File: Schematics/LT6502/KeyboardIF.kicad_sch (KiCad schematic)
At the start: 7 parts, among them J14 KeyConn, U11 W65C51NxQ, X2 1.8432MHz

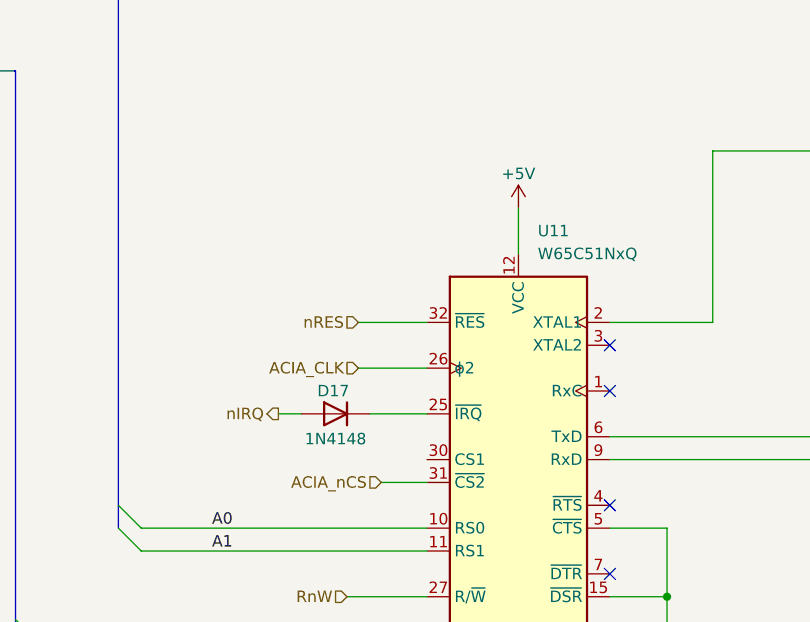
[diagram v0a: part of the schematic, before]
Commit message: Further work on Schematics, All parts placed on PCB
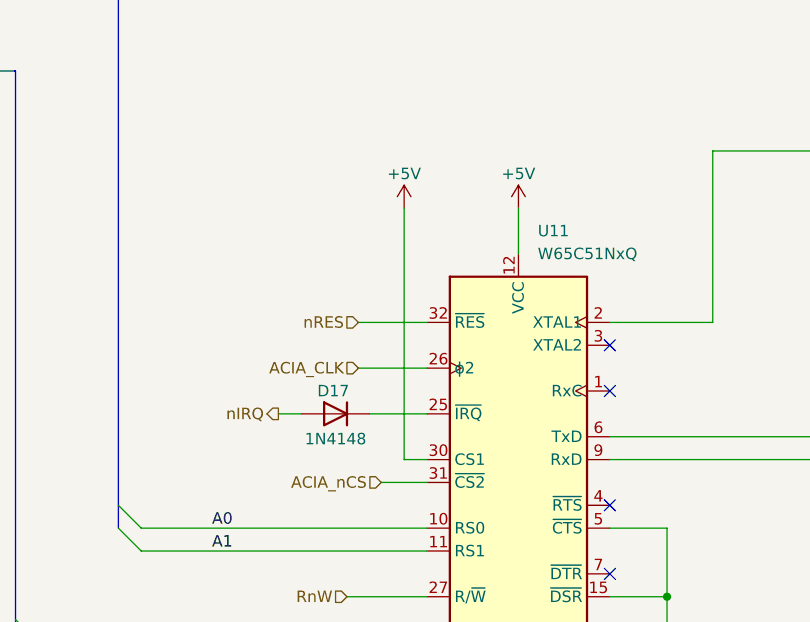
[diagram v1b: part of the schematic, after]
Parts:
- R82: footprint Resistor_SMD:R_0603_1608Metric_Pad0.98x0.95mm_HandSolder -> Resistor_SMD:R_0402_1005Metric
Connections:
- net +5V: now also U11.30 (CS1)
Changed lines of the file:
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@@
+	(wire
+		(pts
+			(xy 135.89 93.98) (xy 135.89 66.04)
+		)
+		(stroke
+			(width 0)
+			(type default)
+		)
+	)
 	(wire
 		(pts
@@
 		(pts
 			(xy 95.25 116.84) (xy 138.43 116.84)
+		)
+		(stroke
+			(width 0)
+			(type default)
+		)
+	)
+	(wire
+		(pts
+			(xy 138.43 93.98) (xy 135.89 93.98)
 		)
 		(stroke
@@
 			)
 		)
-		(property "Footprint" "Resistor_SMD:R_0603_1608Metric_Pad0.98x0.95mm_HandSolder"
+		(property "Footprint" "Resistor_SMD:R_0402_1005Metric"
 			(at 205.232 52.07 90)
 			(effects
@@
 					(unit 1)
 				)
+			)
+		)
+	)
+	(symbol
+		(lib_id "power:+5V")
+		(at 135.89 66.04 0)
+		(mirror y)
+		(unit 1)
+		(exclude_from_sim no)
+		(in_bom yes)
+		(on_board yes)
+		(dnp no)
+		(property "Reference" "#PWR0228"
+			(at 135.89 69.85 0)
+			(effects
+				(font
+					(size 1.27 1.27)
+				)
+				(hide yes)
+			)
+		)
+		(property "Value" "+5V"
+			(at 135.89 62.23 0)
+			(effects
+				(font
+					(size 1.27 1.27)
+				)
+			)
+		)
+		(property "Footprint" ""
+			(at 135.89 66.04 0)
+			(effects
+				(font
+					(size 1.27 1.27)
+				)
+				(hide yes)
+			)
+		)
+		(property "Datasheet" ""
+			(at 135.89 66.04 0)
+			(effects
+				(font
+					(size 1.27 1.27)
+				)
+				(hide yes)
+			)
+		)
+		(property "Description" ""
+			(at 135.89 66.04 0)
+			(effects
+				(font
+					(size 1.27 1.27)
+				)
+			)
+		)
+		(pin "1"
+		)
+		(instances
+			(project "LT6502"
+				(path "/a2243a34-697c-4939-97f7-df548e421864/2b6fed47-3df7-424e-b6fe-61f4842b9a70"
+					(reference "#PWR0228")
+					(unit 1)
+				)

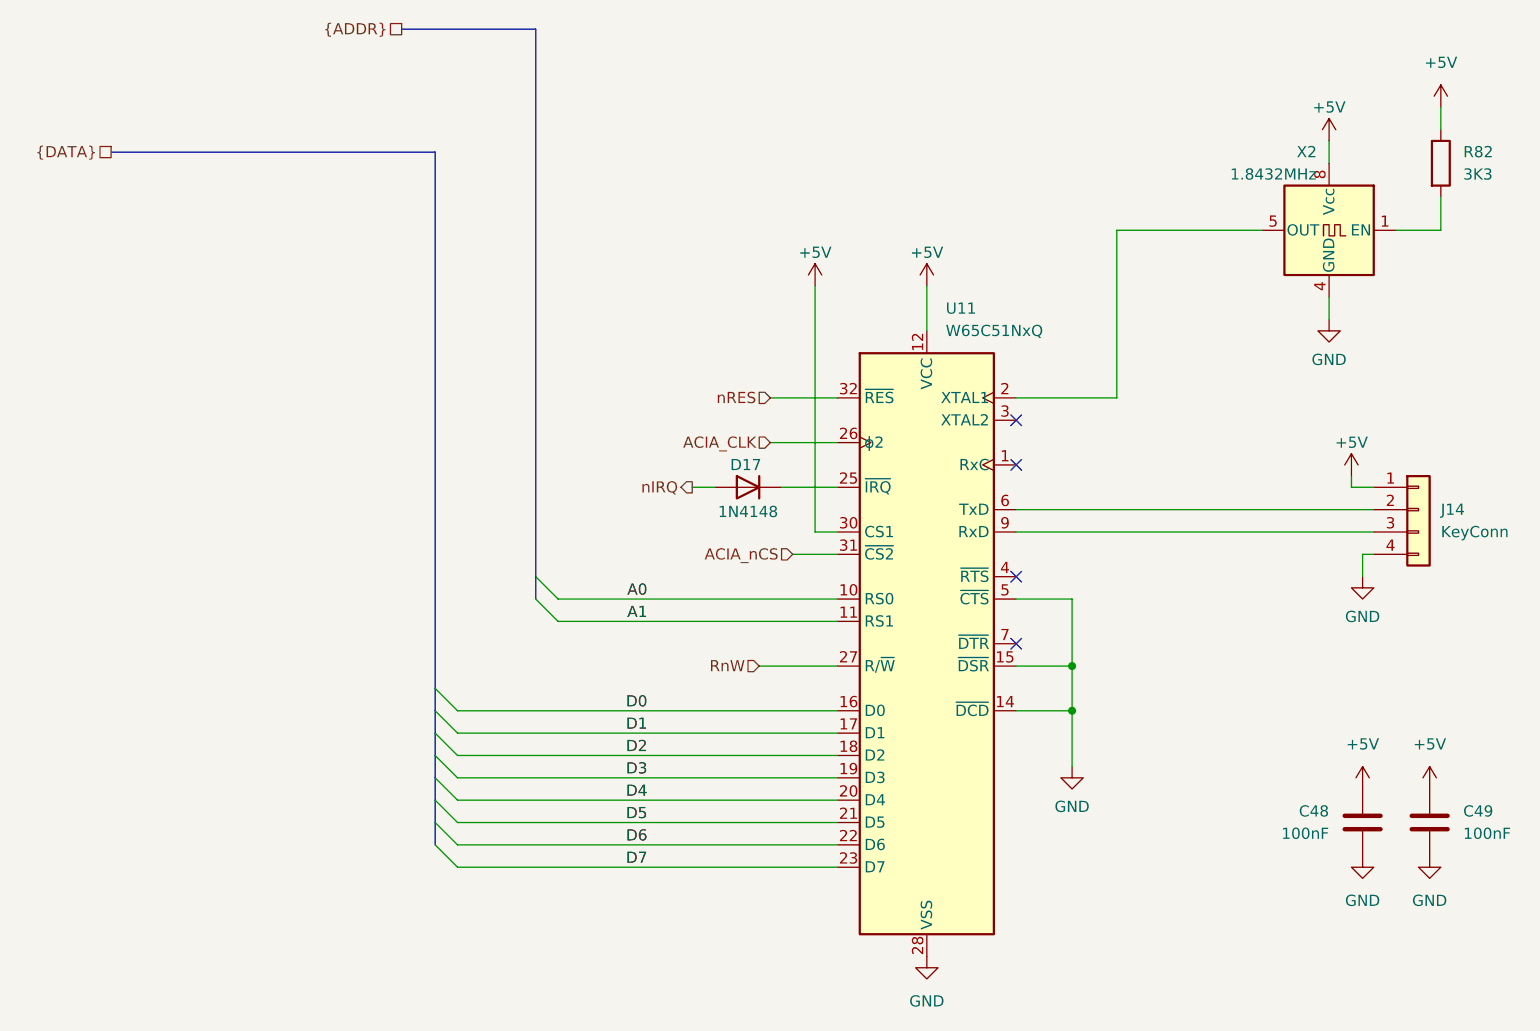
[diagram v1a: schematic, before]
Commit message: Updated main board and started keybed
main board a bit wider due to keybed width
created keybed, begun routing
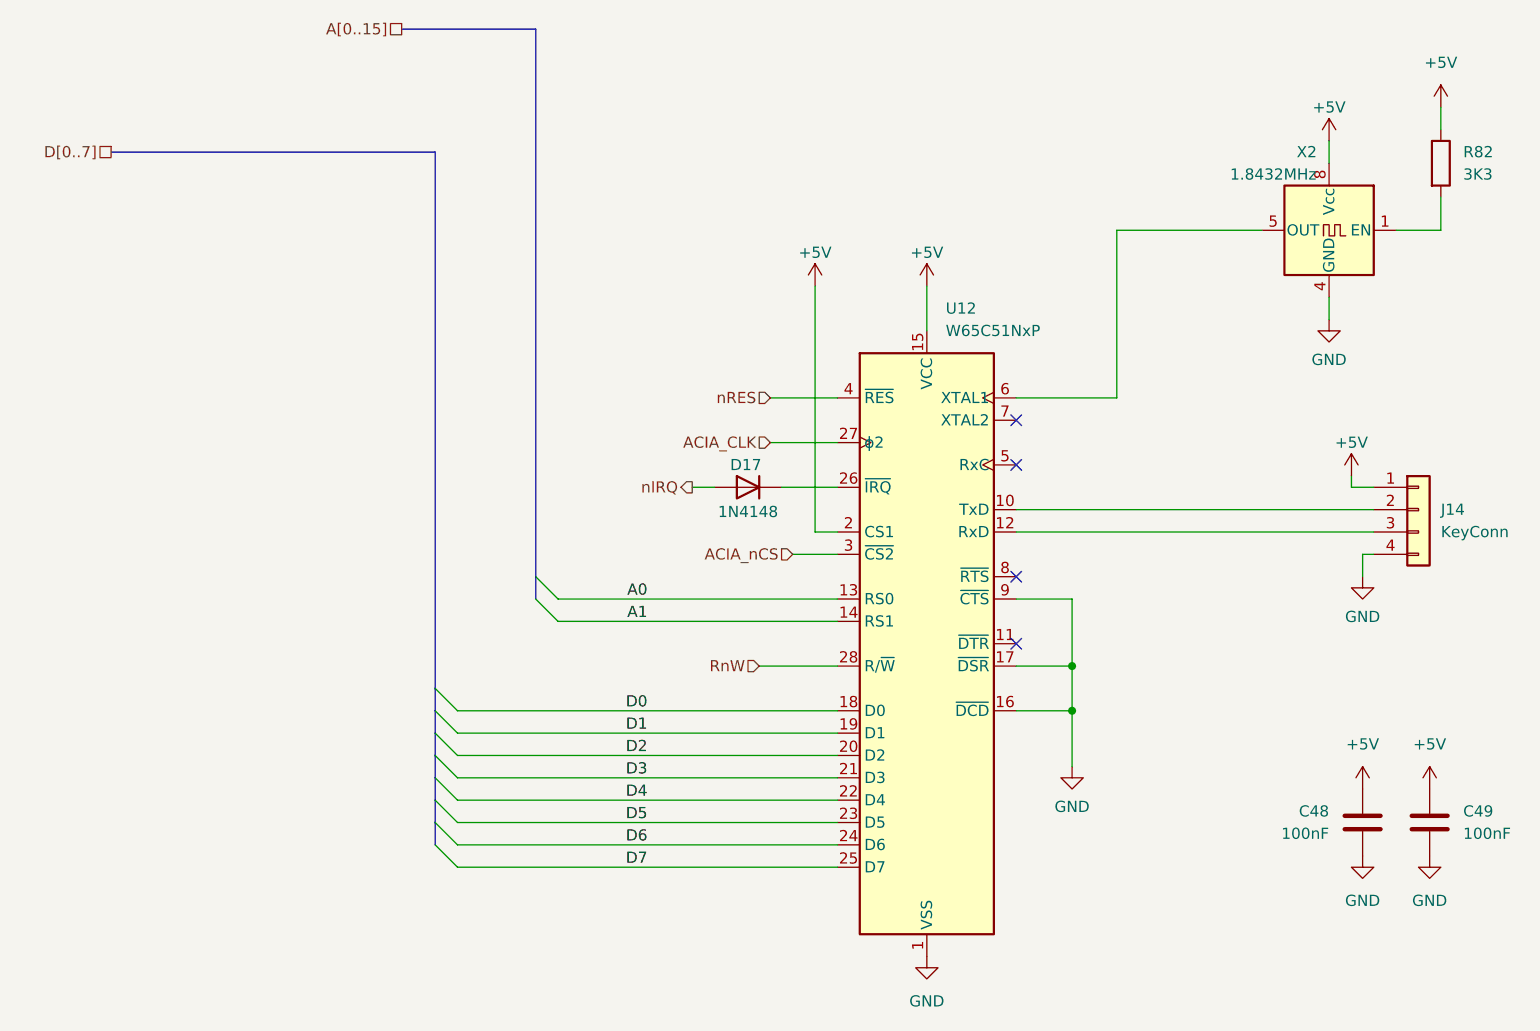
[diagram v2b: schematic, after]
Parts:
- removed U11: W65C51NxQ, Package_QFP:TQFP-32_7x7mm_P0.8mm, symbol 65xx-library:W65C51NxQ
- added U12: W65C51NxP, Package_DIP:DIP-28_W15.24mm, symbol 65xx-library:W65C51NxP
- X2: Mouser Part Number (none) -> 774-MXO45HST-3C-1.8
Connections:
- net +5V: now also U12.15 (VCC), U12.2 (CS1)
- net A0: now also U12.13 (RS0)
- net A1: now also U12.14 (RS1)
- net ACIA_CLK: now also U12.27 (ϕ2)
- net ACIA_nCS: now also U12.3 (~{CS2})
- net D0: now also U12.18 (D0)
- net D1: now also U12.19 (D1)
- net D2: now also U12.20 (D2)
- net D3: now also U12.21 (D3)
- net D4: now also U12.22 (D4)
- net D5: now also U12.23 (D5)
- net D6: now also U12.24 (D6)
- net D7: now also U12.25 (D7)
- net GND: now also U12.1 (VSS), U12.16 (~{DCD}), U12.17 (~{DSR}), U12.9 (~{CTS})
- net RnW: now also U12.28 (R/~{W})
- net nRES: now also U12.4 (~{RES})
- net at X2.5 (OUT): now also U12.6 (XTAL1)
- net at D17.1 (K): now also U12.26 (~{IRQ})
- net at J14.2 (Pin_2): now also U12.10 (TxD)
- net at J14.3 (Pin_3): now also U12.12 (RxD)
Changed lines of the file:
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@@
 		)
 	)
-	(hierarchical_label "{ADDR}"
+	(hierarchical_label "D[0..7]"
+		(shape passive)
+		(at 55.88 50.8 180)
+		(effects
+			(font
+				(size 1.27 1.27)
+			)
+			(justify right)
+		)
+	)
+	(hierarchical_label "A[0..15]"
 		(shape passive)
 		(at 88.9 36.83 180)
@@
 		)
 	)
-	(hierarchical_label "{DATA}"
-		(shape passive)
-		(at 55.88 50.8 180)
-		(effects
-			(font
-				(size 1.27 1.27)
-			)
-			(justify right)
-		)
-	)
 	(hierarchical_label "RnW"
 		(shape input)
@@
 			)
 		)
+		(property "Mouser Part Number" "774-MXO45HST-3C-1.8"
+			(at 194.31 59.69 0)
+			(effects
+				(font
+					(size 1.27 1.27)
+				)
+				(hide yes)
+			)
+		)
 		(pin "1"
 		)
@@
 	)
 	(symbol
+		(lib_id "65xx-library:W65C51NxP")
+		(at 148.59 106.68 0)
+		(unit 1)
+		(exclude_from_sim no)
+		(in_bom yes)
+		(on_board yes)
+		(dnp no)
+		(fields_autoplaced yes)
+		(property "Reference" "U12"
+			(at 150.7333 68.58 0)
+			(effects
+				(font
+					(size 1.27 1.27)
+				)
+				(justify left)
+			)
+		)
+		(property "Value" "W65C51NxP"
+			(at 150.7333 71.12 0)
+			(effects
+				(font
+					(size 1.27 1.27)
+				)
+				(justify left)
+			)
+		)
+		(property "Footprint" "Package_DIP:DIP-28_W15.24mm"
+			(at 148.59 58.42 0)
+			(effects
+				(font
+					(size 1.27 1.27)
+				)
+				(hide yes)
+			)
+		)
+		(property "Datasheet" "http://www.westerndesigncenter.com/wdc/documentation/w65c51n.pdf"
+			(at 148.59 60.96 0)
+			(effects
+				(font
+					(size 1.27 1.27)
+				)
+				(hide yes)
+			)
+		)
+		(property "Description" "CMOS Asynchronous Communication Interface Adapter (ACIA), Serial UART, DIP-28"
+			(at 148.59 106.68 0)
+			(effects
+				(font
+					(size 1.27 1.27)
+				)
+				(hide yes)
+			)
+		)
+		(pin "5"
+		)
+		(pin "18"
+		)
+		(pin "20"
+		)
+		(pin "6"
+		)
+		(pin "19"
+		)
+		(pin "15"
+		)
+		(pin "22"
+		)
+		(pin "8"
+		)
+		(pin "1"
+		)
+		(pin "21"
+		)
+		(pin "24"
+		)
+		(pin "12"
+		)
+		(pin "11"
+		)
+		(pin "26"
+		)
+		(pin "27"
+		)
+		(pin "4"
+		)
+		(pin "28"
+		)
+		(pin "10"
+		)
+		(pin "3"
+		)
+		(pin "14"
+		)
+		(pin "25"
+		)
+		(pin "23"
+		)
+		(pin "16"
+		)
+		(pin "13"
+		)
+		(pin "7"
+		)
+		(pin "2"
+		)
+		(pin "9"
+		)
+		(pin "17"
+		)
+		(instances
+			(project ""
+				(path "/a2243a34-697c-4939-97f7-df548e421864/2b6fed47-3df7-424e-b6fe-61f4842b9a70"
+					(reference "U12")
+					(unit 1)
+				)
+			)
+		)
+	)
+	(symbol
 		(lib_id "power:+5V")
 		(at 207.01 45.72 0)
@@
 					(unit 1)
 				)
-			)
-		)
-	)
-	(symbol
-		(lib_id "65xx-library:W65C51NxQ")
-		(at 148.59 106.68 0)
-		(unit 1)
-		(exclude_from_sim no)
-		(in_bom yes)
-		(on_board yes)
-		(dnp no)
-		(fields_autoplaced yes)
-		(property "Reference" "U11"
-			(at 150.7333 68.58 0)
-			(effects
-				(font
-					(size 1.27 1.27)
-				)
-				(justify left)
-			)
-		)
-		(property "Value" "W65C51NxQ"
-			(at 150.7333 71.12 0)
-			(effects
-				(font
-					(size 1.27 1.27)
-				)
-				(justify left)
-			)
-		)
-		(property "Footprint" "Package_QFP:TQFP-32_7x7mm_P0.8mm"
-			(at 148.59 58.42 0)
-			(effects
-				(font
-					(size 1.27 1.27)
-				)
-				(hide yes)
-			)
-		)
-		(property "Datasheet" "http://www.westerndesigncenter.com/wdc/documentation/w65c51n.pdf"
-			(at 148.59 60.96 0)
-			(effects
-				(font
-					(size 1.27 1.27)
-				)
-				(hide yes)
-			)
-		)
-		(property "Description" "CMOS Asynchronous Communication Interface Adapter (ACIA), Serial UART, LQFP-32"
-			(at 148.59 106.68 0)
-			(effects
-				(font
-					(size 1.27 1.27)
-				)
-				(hide yes)
-			)
-		)
-		(pin "5"
-		)
-		(pin "6"
-		)
-		(pin "1"
-		)
-		(pin "29"
-		)
-		(pin "9"
-		)
-		(pin "13"
-		)
-		(pin "16"
-		)
-		(pin "17"
-		)
-		(pin "10"
-		)
-		(pin "31"
-		)
-		(pin "30"
-		)
-		(pin "2"
-		)
-		(pin "23"
-		)
-		(pin "18"
-		)
-		(pin "7"
-		)
-		(pin "26"
-		)
-		(pin "8"
-		)
-		(pin "4"
-		)
-		(pin "27"
-		)
-		(pin "15"
-		)
-		(pin "14"
-		)
-		(pin "12"
-		)
-		(pin "3"
-		)
-		(pin "21"
-		)
-		(pin "20"
-		)
-		(pin "19"
-		)
-		(pin "25"
-		)
-		(pin "28"
-		)
-		(pin "24"
-		)
-		(pin "11"
-		)
-		(pin "22"
-		)
-		(pin "32"
-		)
-		(instances
-			(project ""
-				(path "/a2243a34-697c-4939-97f7-df548e421864/2b6fed47-3df7-424e-b6fe-61f4842b9a70"
-					(reference "U11")
-					(unit 1)
-				)

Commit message: Updated BoMs ordered PCBs
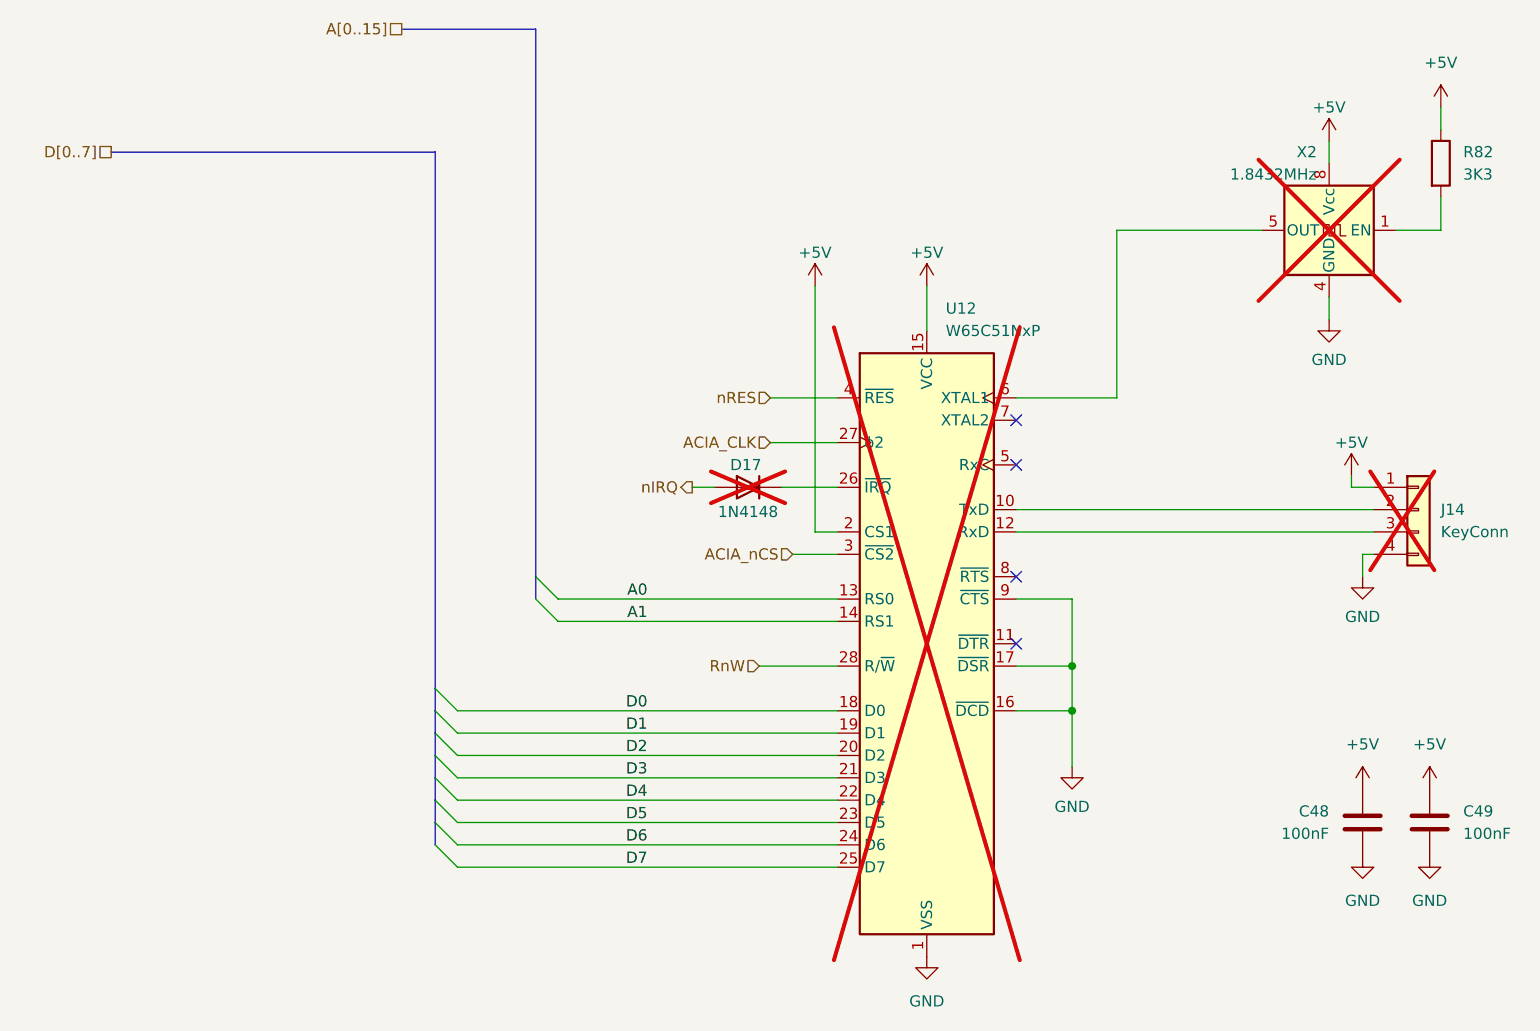
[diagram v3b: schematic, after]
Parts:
- C48, C49: LCSC C49678 -> C113803
- D17, J14, U12: LCSC (none) -> DNF; now not fitted
- X2: now not fitted
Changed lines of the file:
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@@
 		(in_bom yes)
 		(on_board yes)
-		(dnp no)
+		(dnp yes)
 		(property "Reference" "X2"
 			(at 191.77 50.8 0)
@@
 		(in_bom yes)
 		(on_board yes)
-		(dnp no)
+		(dnp yes)
 		(property "Reference" "D17"
 			(at 128.016 86.36 0)
@@
 			)
 		)
+		(property "LCSC" "DNF"
+			(at 128.27 88.9 0)
+			(effects
+				(font
+					(size 1.27 1.27)
+				)
+				(hide yes)
+			)
+		)
 		(pin "2"
 		)
@@
 		(in_bom yes)
 		(on_board yes)
-		(dnp no)
+		(dnp yes)
 		(fields_autoplaced yes)
 		(property "Reference" "U12"
@@
 		)
 		(property "Description" "CMOS Asynchronous Communication Interface Adapter (ACIA), Serial UART, DIP-28"
+			(at 148.59 106.68 0)
+			(effects
+				(font
+					(size 1.27 1.27)
+				)
+				(hide yes)
+			)
+		)
+		(property "LCSC" "DNF"
 			(at 148.59 106.68 0)
 			(effects
@@
 			)
 		)
-		(property "LCSC" "C49678"
+		(property "LCSC" "C113803"
 			(at 205.74 127 0)
 			(effects
@@
 			)
 		)
-		(property "LCSC" "C49678"
+		(property "LCSC" "C113803"
 			(at 198.12 127 0)
 			(effects
@@
 		(in_bom yes)
 		(on_board yes)
-		(dnp no)
+		(dnp yes)
 		(fields_autoplaced yes)
 		(property "Reference" "J14"
@@
 			(at 204.47 91.44 0)
 			(effects
+				(font
+					(size 1.27 1.27)
+				)
+				(hide yes)
+			)
+		)
+		(property "LCSC" "DNF"
+			(at 204.47 91.44 0)
+			(effects

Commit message: Auto stash before merge of "main" and "origin/main"
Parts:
- D17, J14, U12, X2: now fitted
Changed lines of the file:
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@@
 		(in_bom yes)
 		(on_board yes)
-		(dnp yes)
+		(dnp no)
 		(property "Reference" "X2"
 			(at 191.77 50.8 0)
@@
 		(in_bom yes)
 		(on_board yes)
-		(dnp yes)
+		(dnp no)
 		(property "Reference" "D17"
 			(at 128.016 86.36 0)
@@
 		(in_bom yes)
 		(on_board yes)
-		(dnp yes)
+		(dnp no)
 		(fields_autoplaced yes)
 		(property "Reference" "U12"
@@
 		(in_bom yes)
 		(on_board yes)
-		(dnp yes)
+		(dnp no)
 		(fields_autoplaced yes)
 		(property "Reference" "J14"
